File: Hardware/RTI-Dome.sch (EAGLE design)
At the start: 50 parts, among them IC1 24AA128ST, IC2 74LVC244, IC3 FT232RL, IC4 74ABT244, X13 PN61729-S

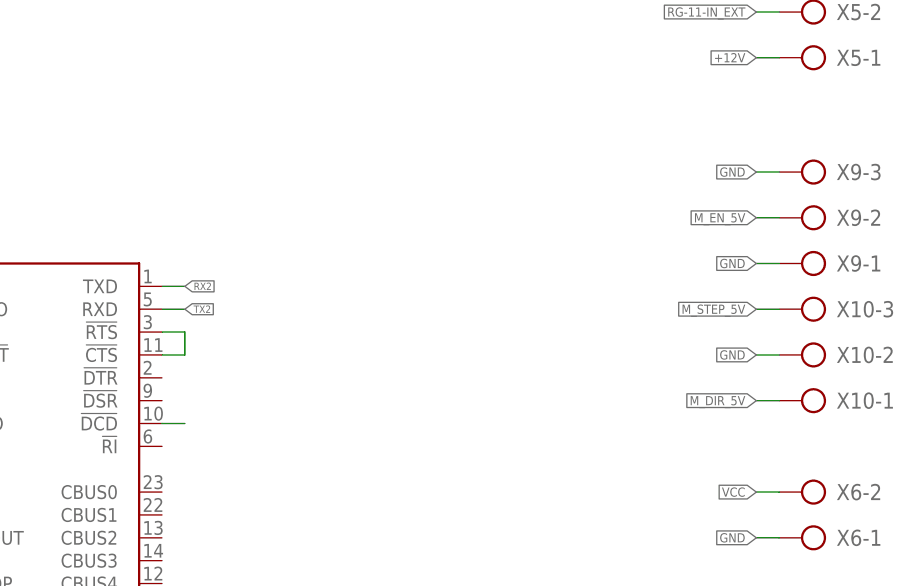
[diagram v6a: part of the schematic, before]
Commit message: Change the polarity on the en.dir,step pin to match the ISD0x too, so no more need to have some #define in the code
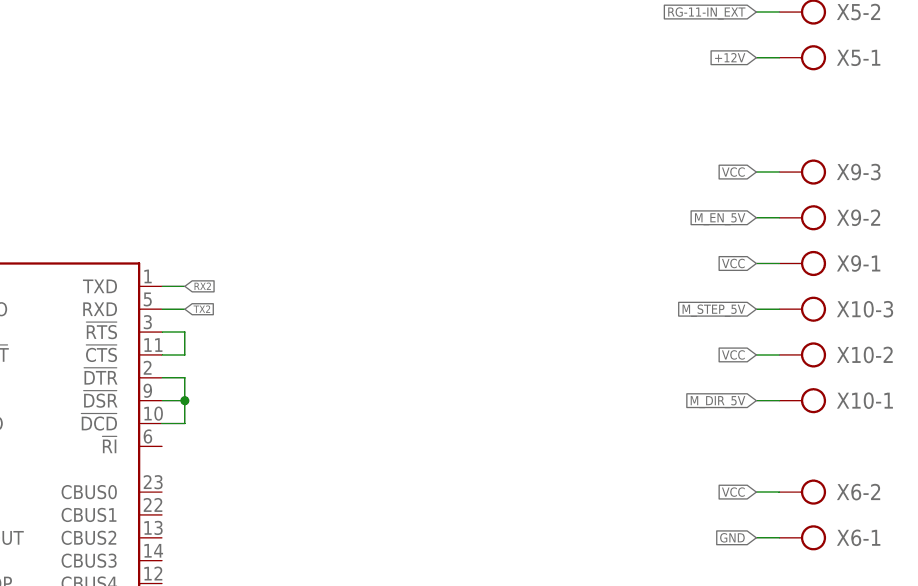
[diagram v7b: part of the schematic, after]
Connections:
- net N$4 renamed RTS_CTS
- removed net N$21: IC3.!DCD
- new net DTR_DSR_DCD: IC3.!DCD, IC3.!DSR, IC3.!DTR
- net GND: no longer X10-2.KL, X9-1.KL, X9-3.KL
- net VCC: now also X10-2.KL, X9-1.KL, X9-3.KL
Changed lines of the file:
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@@
-</segment>
-<segment>
-<wire x1="370.84" y1="185.42" x2="373.38" y2="185.42" width="0.1524" layer="91"/>
-<label x="370.84" y="185.42" size="1.016" layer="95" rot="MR0" xref="yes"/>
-<pinref part="X9" gate="-3" pin="KL"/>
-</segment>
-<segment>
-<wire x1="370.84" y1="175.26" x2="373.38" y2="175.26" width="0.1524" layer="91"/>
-<label x="370.84" y="175.26" size="1.016" layer="95" rot="MR0" xref="yes"/>
-<pinref part="X9" gate="-1" pin="KL"/>
-</segment>
-<segment>
-<wire x1="370.84" y1="165.1" x2="373.38" y2="165.1" width="0.1524" layer="91"/>
-<label x="370.84" y="165.1" size="1.016" layer="95" rot="MR0" xref="yes"/>
-<pinref part="X10" gate="-2" pin="KL"/>
 </segment>
 <segment>
@@
 <pinref part="X6" gate="-2" pin="KL"/>
 </segment>
+<segment>
+<wire x1="370.84" y1="185.42" x2="373.38" y2="185.42" width="0.1524" layer="91"/>
+<label x="370.84" y="185.42" size="1.016" layer="95" rot="MR0" xref="yes"/>
+<pinref part="X9" gate="-3" pin="KL"/>
+</segment>
+<segment>
+<wire x1="370.84" y1="175.26" x2="373.38" y2="175.26" width="0.1524" layer="91"/>
+<label x="370.84" y="175.26" size="1.016" layer="95" rot="MR0" xref="yes"/>
+<pinref part="X9" gate="-1" pin="KL"/>
+</segment>
+<segment>
+<wire x1="370.84" y1="165.1" x2="373.38" y2="165.1" width="0.1524" layer="91"/>
+<label x="370.84" y="165.1" size="1.016" layer="95" rot="MR0" xref="yes"/>
+<pinref part="X10" gate="-2" pin="KL"/>
+</segment>
 </net>
 <net name="N$2" class="0">
@@
 </segment>
 </net>
-<net name="N$21" class="0">
-<segment>
-<pinref part="IC3" gate="1" pin="!DCD"/>
-<wire x1="307.34" y1="157.48" x2="304.8" y2="157.48" width="0.1524" layer="91"/>
-</segment>
-</net>
-<net name="N$4" class="0">
+<net name="RTS_CTS" class="0">
 <segment>
 <pinref part="IC3" gate="1" pin="!RTS"/>
@@
 </segment>
 </net>
+<net name="DTR_DSR_DCD" class="0">
+<segment>
+<pinref part="IC3" gate="1" pin="!DTR"/>
+<wire x1="304.8" y1="162.56" x2="307.34" y2="162.56" width="0.1524" layer="91"/>
+<pinref part="IC3" gate="1" pin="!DSR"/>
+<wire x1="304.8" y1="160.02" x2="307.34" y2="160.02" width="0.1524" layer="91"/>
+<wire x1="307.34" y1="160.02" x2="307.34" y2="162.56" width="0.1524" layer="91"/>
+<pinref part="IC3" gate="1" pin="!DCD"/>
+<wire x1="307.34" y1="157.48" x2="304.8" y2="157.48" width="0.1524" layer="91"/>
+<wire x1="307.34" y1="160.02" x2="307.34" y2="157.48" width="0.1524" layer="91"/>
+<junction x="307.34" y="160.02"/>
+</segment>
+</net>

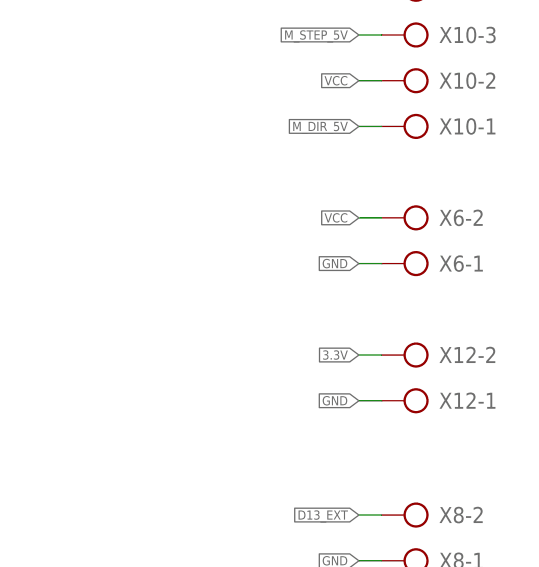
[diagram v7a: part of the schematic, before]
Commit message: Some routing optimisation. Remove 3.3V header as it's not needed anymore. Added 2 ground for good measure
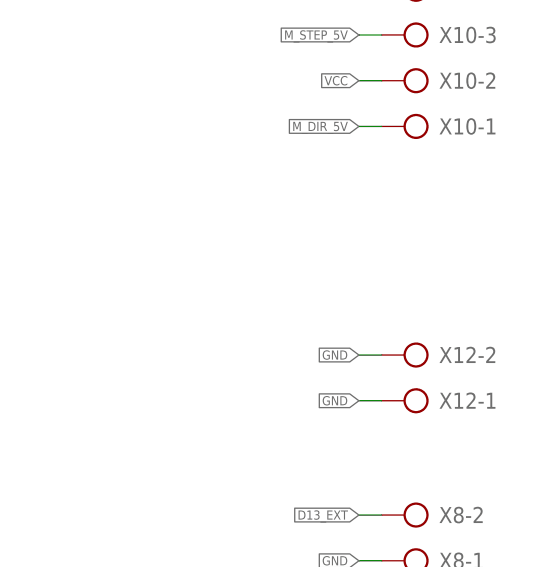
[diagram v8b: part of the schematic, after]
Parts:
- removed X6: (no value), con-ptr500:AK500/2
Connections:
- net 3.3V: no longer X12-2.KL
- net GND: now also X12-2.KL; no longer X6-1.KL
- net VCC: no longer X6-2.KL
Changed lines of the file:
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@@
 <part name="XB1" library="maxstream" deviceset="XBEE" device=""/>
 <part name="GND6" library="supply1" deviceset="GND" device=""/>
-<part name="X6" library="con-ptr500" deviceset="AK500/2" device=""/>
 <part name="PCB1" library="arduino_shield" deviceset="ARDUINO_DUE_SHIELD_SHORT" device=""/>
 <part name="R2" library="rti" deviceset="R-EU" device="'0805'" value="100K 0.1%"/>
@@
 <instance part="XB1" gate="G$1" x="165.1" y="55.88"/>
 <instance part="GND6" gate="1" x="147.32" y="22.86"/>
-<instance part="X6" gate="-1" x="378.46" y="144.78" rot="R180"/>
-<instance part="X6" gate="-2" x="378.46" y="149.86" rot="R180"/>
 <instance part="PCB1" gate="G$1" x="53.34" y="38.1" rot="R270"/>
 <instance part="R2" gate="G$1" x="7.62" y="213.36" rot="R90"/>
@@
 </segment>
 <segment>
-<wire x1="370.84" y1="144.78" x2="373.38" y2="144.78" width="0.1524" layer="91"/>
-<label x="370.84" y="144.78" size="1.016" layer="95" rot="R180" xref="yes"/>
-<pinref part="X6" gate="-1" pin="KL"/>
-</segment>
-<segment>
 <pinref part="IC2" gate="G$1" pin="2A2"/>
 <wire x1="116.84" y1="231.14" x2="119.38" y2="231.14" width="0.1524" layer="91"/>
@@
 <wire x1="187.96" y1="220.98" x2="190.5" y2="220.98" width="0.1524" layer="91"/>
 <label x="187.96" y="220.98" size="0.8128" layer="95" rot="R180" xref="yes"/>
+</segment>
+<segment>
+<pinref part="X12" gate="-2" pin="KL"/>
+<wire x1="370.84" y1="134.62" x2="373.38" y2="134.62" width="0.1524" layer="91"/>
+<label x="370.84" y="134.62" size="1.016" layer="95" rot="R180" xref="yes"/>
 </segment>
 </net>
@@
 <wire x1="264.16" y1="170.18" x2="264.16" y2="175.26" width="0.1524" layer="91"/>
 <label x="264.16" y="175.26" size="1.016" layer="95" rot="R90" xref="yes"/>
-</segment>
-<segment>
-<pinref part="X12" gate="-2" pin="KL"/>
-<wire x1="370.84" y1="134.62" x2="373.38" y2="134.62" width="0.1524" layer="91"/>
-<label x="370.84" y="134.62" size="1.016" layer="95" rot="R180" xref="yes"/>
 </segment>
 </net>
@@
 </segment>
 <segment>
-<wire x1="370.84" y1="149.86" x2="373.38" y2="149.86" width="0.1524" layer="91"/>
-<label x="370.84" y="149.86" size="1.016" layer="95" rot="R180" xref="yes"/>
-<pinref part="X6" gate="-2" pin="KL"/>
-</segment>
-<segment>
